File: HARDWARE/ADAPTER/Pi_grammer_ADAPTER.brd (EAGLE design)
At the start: 15.2 x 21.6 mm, 3 parts, among them J3 TESTBED, J4 CABLE

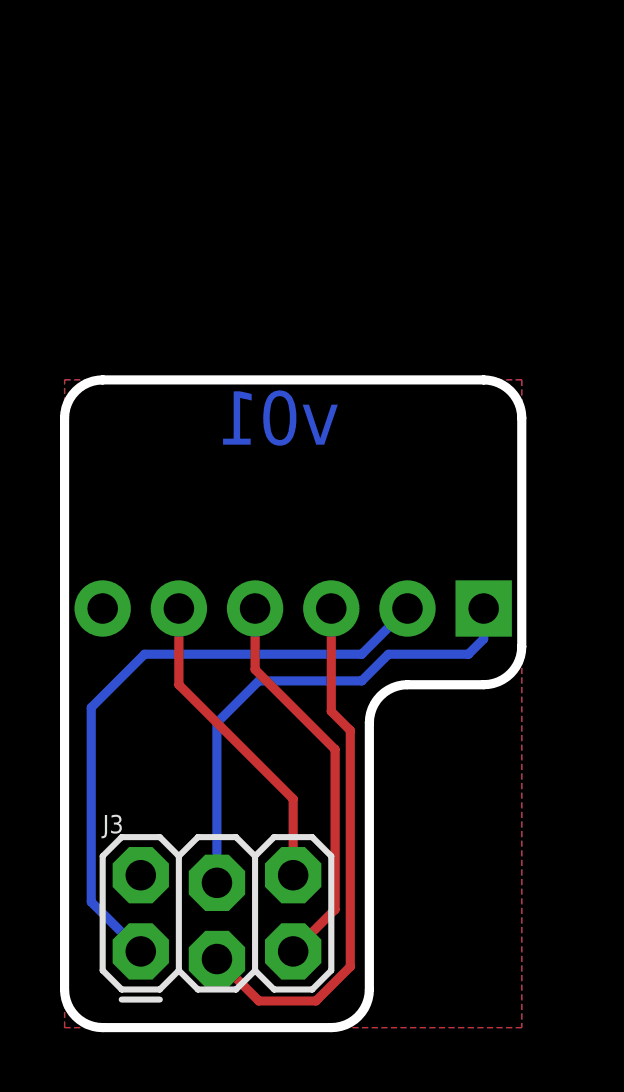
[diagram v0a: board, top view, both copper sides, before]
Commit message: Option to "tap" logic level from target
Note, this required a modification to the ADAPTER as well. I am
utilizing pin 6 on the 1x6 pin header (jumper wire) to transfer VCC back
to the logic level converter.

I'm not sure why on the original design I didn't think to include VCC in
the comm lines to the target - I think it was because the raspi doesn't
have any ADCs to actually  verify it, so I didn't know if it was worth
it.
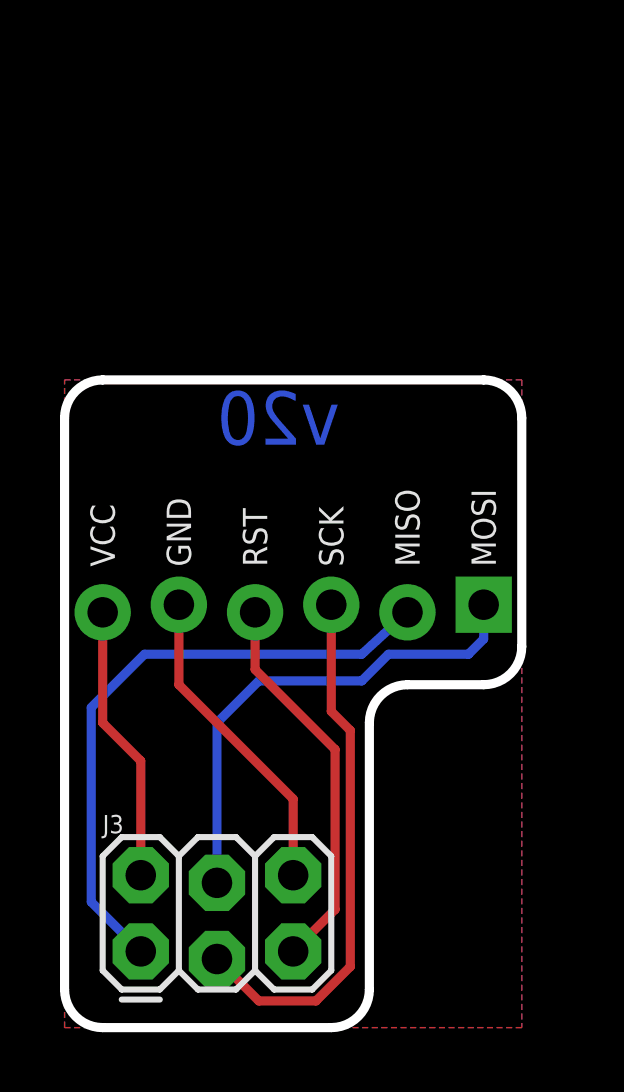
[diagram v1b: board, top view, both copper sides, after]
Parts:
- J4: device SparkFun-Connectors:MOLEX-1X6-RA -> SparkFun-Connectors:MOLEX_1X6_RA_LOCK
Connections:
- new net VCC_C: J3.2, J4.6
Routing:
- net VCC_C: track 0.00 -> 9.29 mm
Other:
- board text added: "GND"
- board text added: "MISO"
- board text added: "MOSI"
- board text added: "RST"
- board text added: "SCK"
- board text added: "VCC"
- board text added: "v20"
- board text removed: "v01"
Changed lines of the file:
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@@
 <layer number="47" name="Measures" color="7" fill="1" visible="no" active="yes"/>
 <layer number="48" name="Document" color="7" fill="1" visible="no" active="yes"/>
-<layer number="49" name="Reference" color="7" fill="1" visible="yes" active="yes"/>
+<layer number="49" name="Reference" color="7" fill="1" visible="no" active="yes"/>
 <layer number="50" name="dxf" color="7" fill="1" visible="no" active="yes"/>
 <layer number="51" name="tDocu" color="6" fill="1" visible="yes" active="yes"/>
@@
 <wire x1="10.16" y1="10.16" x2="10.16" y2="1.27" width="0.3048" layer="20"/>
 <text x="8.89" y="-12.7" size="1.778" layer="51" font="vector">Pete Lewis</text>
-<text x="5.08" y="20.32" size="1.778" layer="16" font="vector" ratio="21" rot="MR0" align="center-right">v01</text>
+<text x="5.08" y="20.32" size="1.778" layer="16" font="vector" ratio="21" rot="MR0" align="center-right">v20</text>
+<text x="13.97" y="15.367" size="0.8128" layer="21" font="vector" ratio="15" rot="R270" align="center-right">MOSI</text>
+<text x="11.43" y="15.367" size="0.8128" layer="21" font="vector" ratio="15" rot="R270" align="center-right">MISO</text>
+<text x="8.89" y="15.367" size="0.8128" layer="21" font="vector" ratio="15" rot="R270" align="center-right">SCK</text>
+<text x="6.35" y="15.367" size="0.8128" layer="21" font="vector" ratio="15" rot="R270" align="center-right">RST</text>
+<text x="3.81" y="15.367" size="0.8128" layer="21" font="vector" ratio="15" rot="R270" align="center-right">GND</text>
+<text x="1.27" y="15.367" size="0.8128" layer="21" font="vector" ratio="15" rot="R270" align="center-right">VCC</text>
 </plain>
 <attributes>
@@
 <attribute name="PROD_ID" value="CONN-11566" x="2.54" y="2.54" size="1.778" layer="27" display="off"/>
 </element>
-<element name="J4" library="SparkFun-Connectors" package="MOLEX-1X6-RA" value="CABLE" x="13.97" y="13.97" rot="MR0">
+<element name="J4" library="SparkFun-Connectors" package="MOLEX_1X6_RA_LOCK" value="CABLE" x="13.97" y="13.97" rot="MR0">
 <attribute name="PROD_ID" value="CONN-10140" x="13.97" y="13.97" size="1.778" layer="28" rot="MR0" display="off"/>
 </element>
@@
 <contactref element="J4" pad="1"/>
 <contactref element="J3" pad="4"/>
-<wire x1="13.97" y1="13.97" x2="13.97" y2="12.954" width="0.3048" layer="16"/>
+<wire x1="13.97" y1="14.097" x2="13.97" y2="12.954" width="0.3048" layer="16"/>
 <wire x1="13.97" y1="12.954" x2="13.462" y2="12.446" width="0.3048" layer="16"/>
 <wire x1="13.462" y1="12.446" x2="10.795" y2="12.446" width="0.3048" layer="16"/>
@@
 <contactref element="J4" pad="2"/>
 <contactref element="J3" pad="1"/>
-<wire x1="11.43" y1="13.97" x2="9.906" y2="12.446" width="0.3048" layer="16"/>
+<wire x1="11.43" y1="13.843" x2="9.906" y2="12.446" width="0.3048" layer="16"/>
 <wire x1="9.906" y1="12.446" x2="2.667" y2="12.446" width="0.3048" layer="16"/>
 <wire x1="2.667" y1="12.446" x2="0.889" y2="10.668" width="0.3048" layer="16"/>
@@
 <contactref element="J3" pad="3"/>
 <contactref element="J4" pad="3"/>
-<wire x1="8.89" y1="13.97" x2="8.89" y2="10.541" width="0.3048" layer="1"/>
+<wire x1="8.89" y1="14.097" x2="8.89" y2="10.541" width="0.3048" layer="1"/>
 <wire x1="8.89" y1="10.541" x2="9.525" y2="9.906" width="0.3048" layer="1"/>
 <wire x1="9.525" y1="9.906" x2="9.525" y2="2.032" width="0.3048" layer="1"/>
@@
 <contactref element="J4" pad="4"/>
 <contactref element="J3" pad="5"/>
-<wire x1="6.35" y1="13.97" x2="6.35" y2="11.938" width="0.3048" layer="1"/>
+<wire x1="6.35" y1="13.843" x2="6.35" y2="11.938" width="0.3048" layer="1"/>
 <wire x1="9.017" y1="9.271" x2="9.017" y2="3.937" width="0.3048" layer="1"/>
 <wire x1="9.017" y1="3.937" x2="7.62" y2="2.54" width="0.3048" layer="1"/>
@@
 <contactref element="J4" pad="5"/>
 <contactref element="J3" pad="6"/>
-<wire x1="3.81" y1="13.97" x2="3.81" y2="11.43" width="0.3048" layer="1"/>
+<wire x1="3.81" y1="14.097" x2="3.81" y2="11.43" width="0.3048" layer="1"/>
 <polygon width="0.3048" layer="16" isolate="0.3048">
 <vertex x="15.24" y="0"/>
@@
 <wire x1="7.62" y1="7.62" x2="7.62" y2="5.08" width="0.3048" layer="1"/>
 </signal>
+<signal name="VCC_C">
+<contactref element="J3" pad="2"/>
+<contactref element="J4" pad="6"/>
+<wire x1="1.27" y1="13.843" x2="1.27" y2="10.16" width="0.3048" layer="1"/>
+<wire x1="1.27" y1="10.16" x2="2.54" y2="8.89" width="0.3048" layer="1"/>
+<wire x1="2.54" y1="8.89" x2="2.54" y2="5.08" width="0.3048" layer="1"/>
+</signal>
 </signals>

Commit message: moved 1x6 header to allow for RA header
This should allow for the cable to flow directly downward from the
pi_grammer and sit with a lower profile. This should help prevent the
cable/header from getting knocked around during handling.

Also had to update the adapter - rotated header 180 degrees so it will
mate straight pin-to-pin on the 1x6 header on the speedySPI.
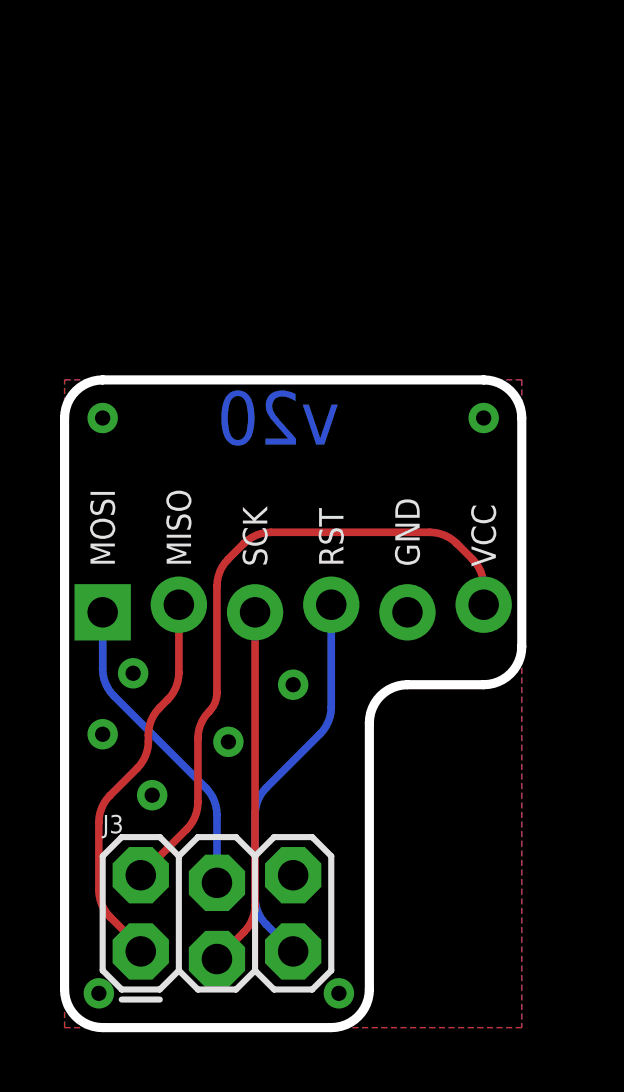
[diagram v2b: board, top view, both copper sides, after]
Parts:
- moved J4 12.7 mm to (1.27, 14.0), turned to 180 degrees
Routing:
- net VCC_C: track 9.29 -> 21.8 mm
- net GND_C: track 10.6 -> 0.00 mm, vias 0 -> 9
- net MISO_C: track 20.6 -> 12.8 mm
- net MOSI_C: track 16.5 -> 10.4 mm
- net SCK_C: track 17.8 -> 12.0 mm

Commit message: Adapter updates for storefront product
-Added open source hardware logo
-sparkfun flame
-"product" board name
-schematic cleanup
-removed rounded cornders for easier board de-panelization
-lengthened board to eliiminate overhaning parts
-moved to SMT parts for easier assembly
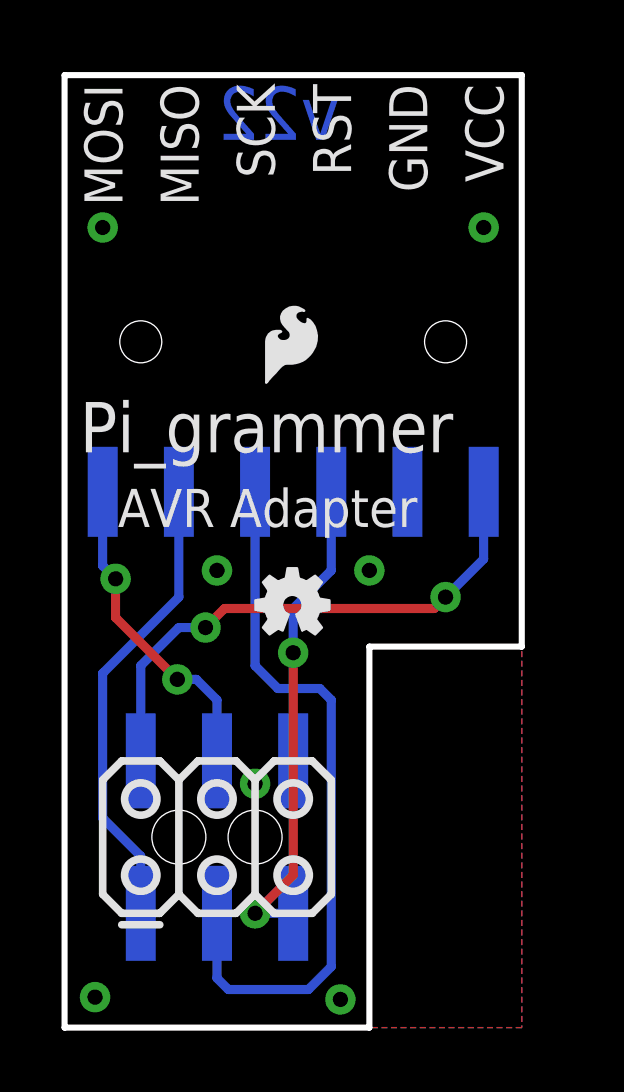
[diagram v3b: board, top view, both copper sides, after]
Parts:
- removed J3: TESTBED, SparkFun-Connectors:2X3_LOCK
- removed J4: CABLE, SparkFun-Connectors:MOLEX_1X6_RA_LOCK
- added J1: AVR 3X2 TARGET, SparkFun-Connectors:2X3_SMT_POSTS
- added J2: CABLE, SparkFun-Connectors:1X06-SMD_RA_MALE
- added LOGO1: SFE_LOGO_FLAME.1_INCH, SparkFun-Aesthetics:SFE_LOGO_FLAME_.1
- added LOGO2: OSHW-LOGOMINI, SparkFun-Aesthetics:OSHW-LOGO-MINI
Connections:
- net GND_C: now also J1.5, J2.5; no longer J3.6, J4.5
- net MISO_C: now also J1.2, J2.2; no longer J3.1, J4.2
- net MOSI_C: now also J1.3, J2.1; no longer J3.4, J4.1
- net RST_C: now also J1.6, J2.4; no longer J3.5, J4.4
- net SCK_C: now also J1.4, J2.3; no longer J3.3, J4.3
- net VCC_C: now also J1.1, J2.6; no longer J3.2, J4.6
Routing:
- net SCK_C: track 12.0 -> 24.1 mm
- net RST_C: track 12.9 -> 16.4 mm, vias 0 -> 2
- net VCC_C: track 21.8 -> 18.3 mm, vias 0 -> 2
- net MISO_C: track 12.8 -> 15.6 mm
- net MOSI_C: track 10.4 -> 10.9 mm, vias 0 -> 2
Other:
- board size 15.2 x 21.6 mm -> 15.2 x 31.8 mm
- board text added: "AVR Adapter"
- board text added: "Pi_grammer"
- board text added: "v22"
- board text removed: "v20"
